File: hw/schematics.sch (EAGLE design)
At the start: 50 parts, among them Q2 MOSFET-NCHANNEL2N7000, Q3 IRF9530, Q4 MOSFET-NCHANNEL2N7000, Q5 IRF9530, Q6 MOSFET-NCHANNEL2N7000, Q7 IRF9530, Q8 MOSFET-NCHANNEL2N7000, Q9 IRF9530, X1 22-23-2031, X2 22-23-2021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

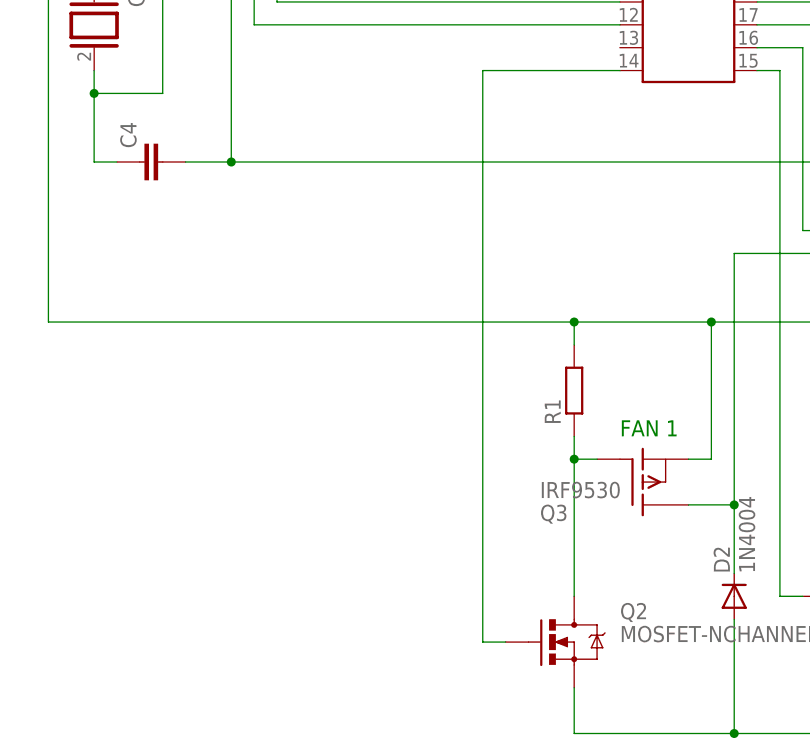
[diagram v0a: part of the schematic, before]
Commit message: Add missing ground connection to output MOSFET switches
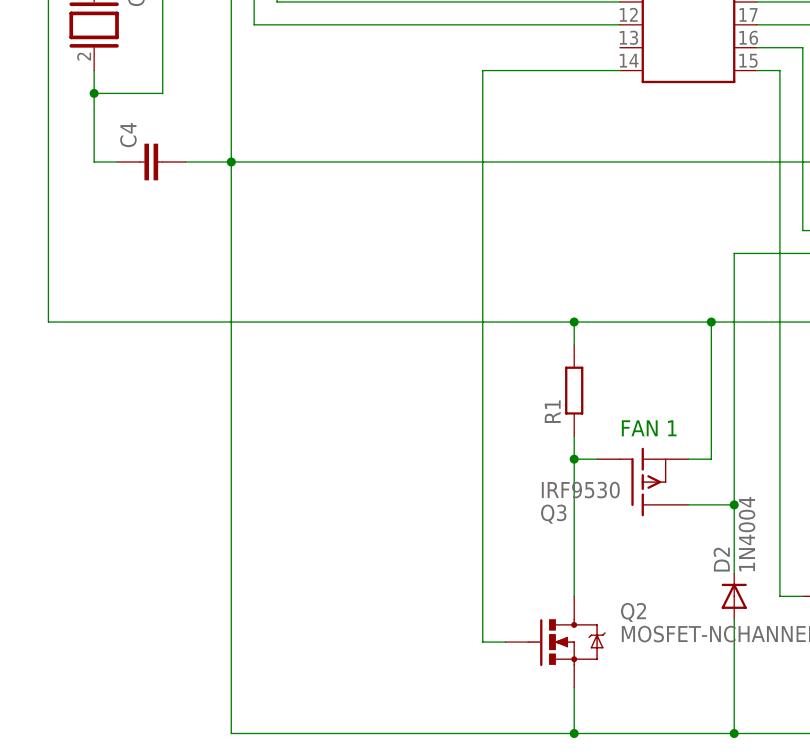
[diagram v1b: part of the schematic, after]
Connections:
- removed net N$8: D2.A, D3.A, D4.A, D5.A, Q2.S, Q4.S, Q6.S, Q8.S
- net N$7: now also D2.A, D3.A, D4.A, D5.A, Q2.S, Q4.S, Q6.S, Q8.S
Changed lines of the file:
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@@
 <?xml version="1.0" encoding="utf-8"?>
 <!DOCTYPE eagle SYSTEM "eagle.dtd">
-<eagle version="6.5.0">
+<eagle version="6.6.0">
 <drawing>
 <settings>
@@
 </segment>
 </net>
-<net name="N$8" class="0">
-<segment>
-<wire x1="33.02" y1="-25.4" x2="50.8" y2="-25.4" width="0.1524" layer="91"/>
-<wire x1="50.8" y1="-25.4" x2="66.04" y2="-25.4" width="0.1524" layer="91"/>
-<wire x1="66.04" y1="-25.4" x2="83.82" y2="-25.4" width="0.1524" layer="91"/>
-<wire x1="83.82" y1="-25.4" x2="104.14" y2="-25.4" width="0.1524" layer="91"/>
-<wire x1="104.14" y1="-25.4" x2="121.92" y2="-25.4" width="0.1524" layer="91"/>
-<junction x="66.04" y="-25.4"/>
-<junction x="104.14" y="-25.4"/>
-<pinref part="Q2" gate="G$1" pin="S"/>
-<wire x1="121.92" y1="-25.4" x2="134.62" y2="-25.4" width="0.1524" layer="91"/>
-<wire x1="33.02" y1="-20.32" x2="33.02" y2="-25.4" width="0.1524" layer="91"/>
-<pinref part="Q4" gate="G$1" pin="S"/>
-<wire x1="66.04" y1="-25.4" x2="66.04" y2="-15.24" width="0.1524" layer="91"/>
-<pinref part="Q6" gate="G$1" pin="S"/>
-<wire x1="104.14" y1="-25.4" x2="104.14" y2="-20.32" width="0.1524" layer="91"/>
-<pinref part="Q8" gate="G$1" pin="S"/>
-<wire x1="134.62" y1="-25.4" x2="134.62" y2="-15.24" width="0.1524" layer="91"/>
-<pinref part="D2" gate="1" pin="A"/>
-<wire x1="50.8" y1="-12.7" x2="50.8" y2="-25.4" width="0.1524" layer="91"/>
-<junction x="50.8" y="-25.4"/>
-<pinref part="D3" gate="1" pin="A"/>
-<wire x1="83.82" y1="-15.24" x2="83.82" y2="-25.4" width="0.1524" layer="91"/>
-<pinref part="D5" gate="1" pin="A"/>
-<wire x1="152.4" y1="-15.24" x2="152.4" y2="-25.4" width="0.1524" layer="91"/>
-<wire x1="152.4" y1="-25.4" x2="134.62" y2="-25.4" width="0.1524" layer="91"/>
-<pinref part="D4" gate="1" pin="A"/>
-<wire x1="121.92" y1="-15.24" x2="121.92" y2="-25.4" width="0.1524" layer="91"/>
-<junction x="83.82" y="-25.4"/>
-<junction x="121.92" y="-25.4"/>
-<junction x="134.62" y="-25.4"/>
-</segment>
-</net>
 <net name="N$9" class="0">
 <segment>
@@
 <wire x1="76.2" y1="38.1" x2="68.58" y2="38.1" width="0.1524" layer="91"/>
 <junction x="68.58" y="38.1"/>
-</segment>
-</net>
+<wire x1="-5.08" y1="38.1" x2="-5.08" y2="-25.4" width="0.1524" layer="91"/>
+<wire x1="33.02" y1="-25.4" x2="50.8" y2="-25.4" width="0.1524" layer="91"/>
+<wire x1="50.8" y1="-25.4" x2="66.04" y2="-25.4" width="0.1524" layer="91"/>
+<wire x1="66.04" y1="-25.4" x2="83.82" y2="-25.4" width="0.1524" layer="91"/>
+<wire x1="83.82" y1="-25.4" x2="104.14" y2="-25.4" width="0.1524" layer="91"/>
+<wire x1="104.14" y1="-25.4" x2="121.92" y2="-25.4" width="0.1524" layer="91"/>
+<junction x="66.04" y="-25.4"/>
+<junction x="104.14" y="-25.4"/>
+<pinref part="Q2" gate="G$1" pin="S"/>
+<wire x1="121.92" y1="-25.4" x2="134.62" y2="-25.4" width="0.1524" layer="91"/>
+<wire x1="33.02" y1="-20.32" x2="33.02" y2="-25.4" width="0.1524" layer="91"/>
+<pinref part="Q4" gate="G$1" pin="S"/>
+<wire x1="66.04" y1="-25.4" x2="66.04" y2="-15.24" width="0.1524" layer="91"/>
+<pinref part="Q6" gate="G$1" pin="S"/>
+<wire x1="104.14" y1="-25.4" x2="104.14" y2="-20.32" width="0.1524" layer="91"/>
+<pinref part="Q8" gate="G$1" pin="S"/>
+<wire x1="134.62" y1="-25.4" x2="134.62" y2="-15.24" width="0.1524" layer="91"/>
+<pinref part="D2" gate="1" pin="A"/>
+<wire x1="50.8" y1="-12.7" x2="50.8" y2="-25.4" width="0.1524" layer="91"/>
+<junction x="50.8" y="-25.4"/>
+<pinref part="D3" gate="1" pin="A"/>
+<wire x1="83.82" y1="-15.24" x2="83.82" y2="-25.4" width="0.1524" layer="91"/>
+<pinref part="D5" gate="1" pin="A"/>
+<wire x1="152.4" y1="-15.24" x2="152.4" y2="-25.4" width="0.1524" layer="91"/>
+<wire x1="152.4" y1="-25.4" x2="134.62" y2="-25.4" width="0.1524" layer="91"/>
+<pinref part="D4" gate="1" pin="A"/>
+<wire x1="121.92" y1="-15.24" x2="121.92" y2="-25.4" width="0.1524" layer="91"/>
+<junction x="83.82" y="-25.4"/>
+<junction x="121.92" y="-25.4"/>
+<junction x="134.62" y="-25.4"/>
+<wire x1="-5.08" y1="-25.4" x2="33.02" y2="-25.4" width="0.1524" layer="91"/>
+<junction x="33.02" y="-25.4"/>
+</segment>
+</net>
